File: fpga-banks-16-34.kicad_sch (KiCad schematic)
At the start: 45 parts, among them U1 ASFLMB-100.000MHZ-XY-T, U15 XC7K160T-FFG676, U8 PCA9517ADMR2G

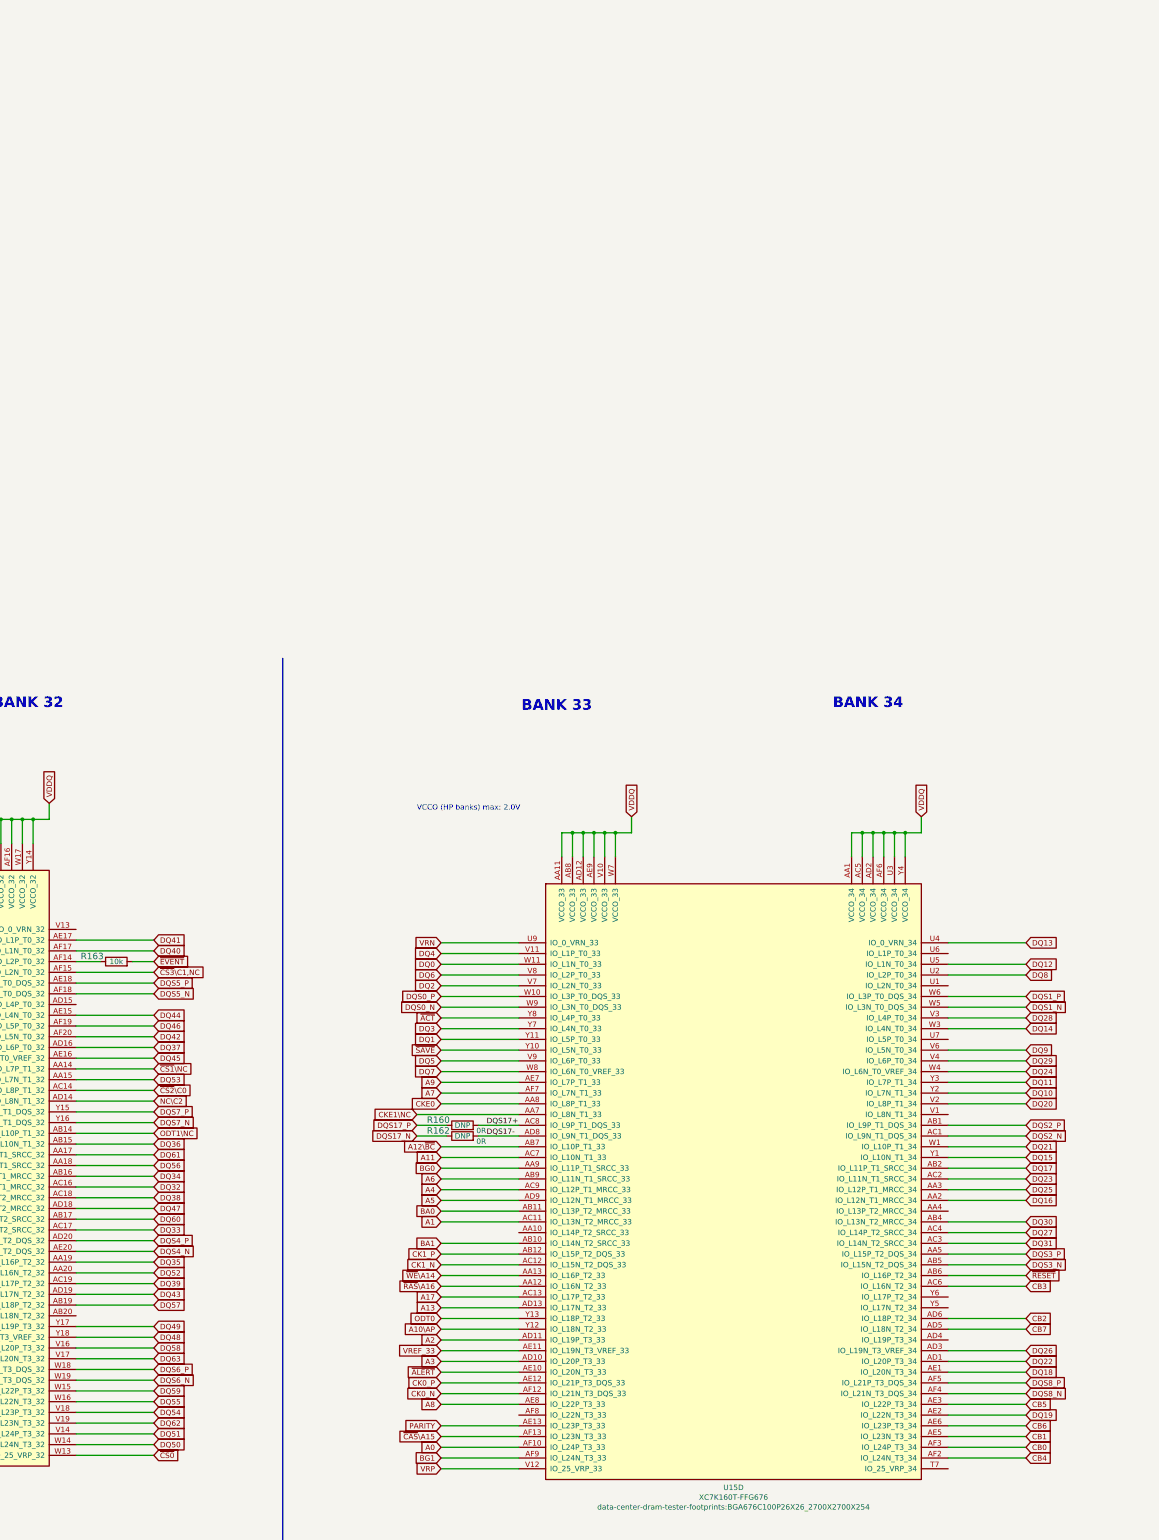
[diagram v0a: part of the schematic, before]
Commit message: Propose optimized DDR4 pinout for die[6..9], initial BGA fanout for bank 32
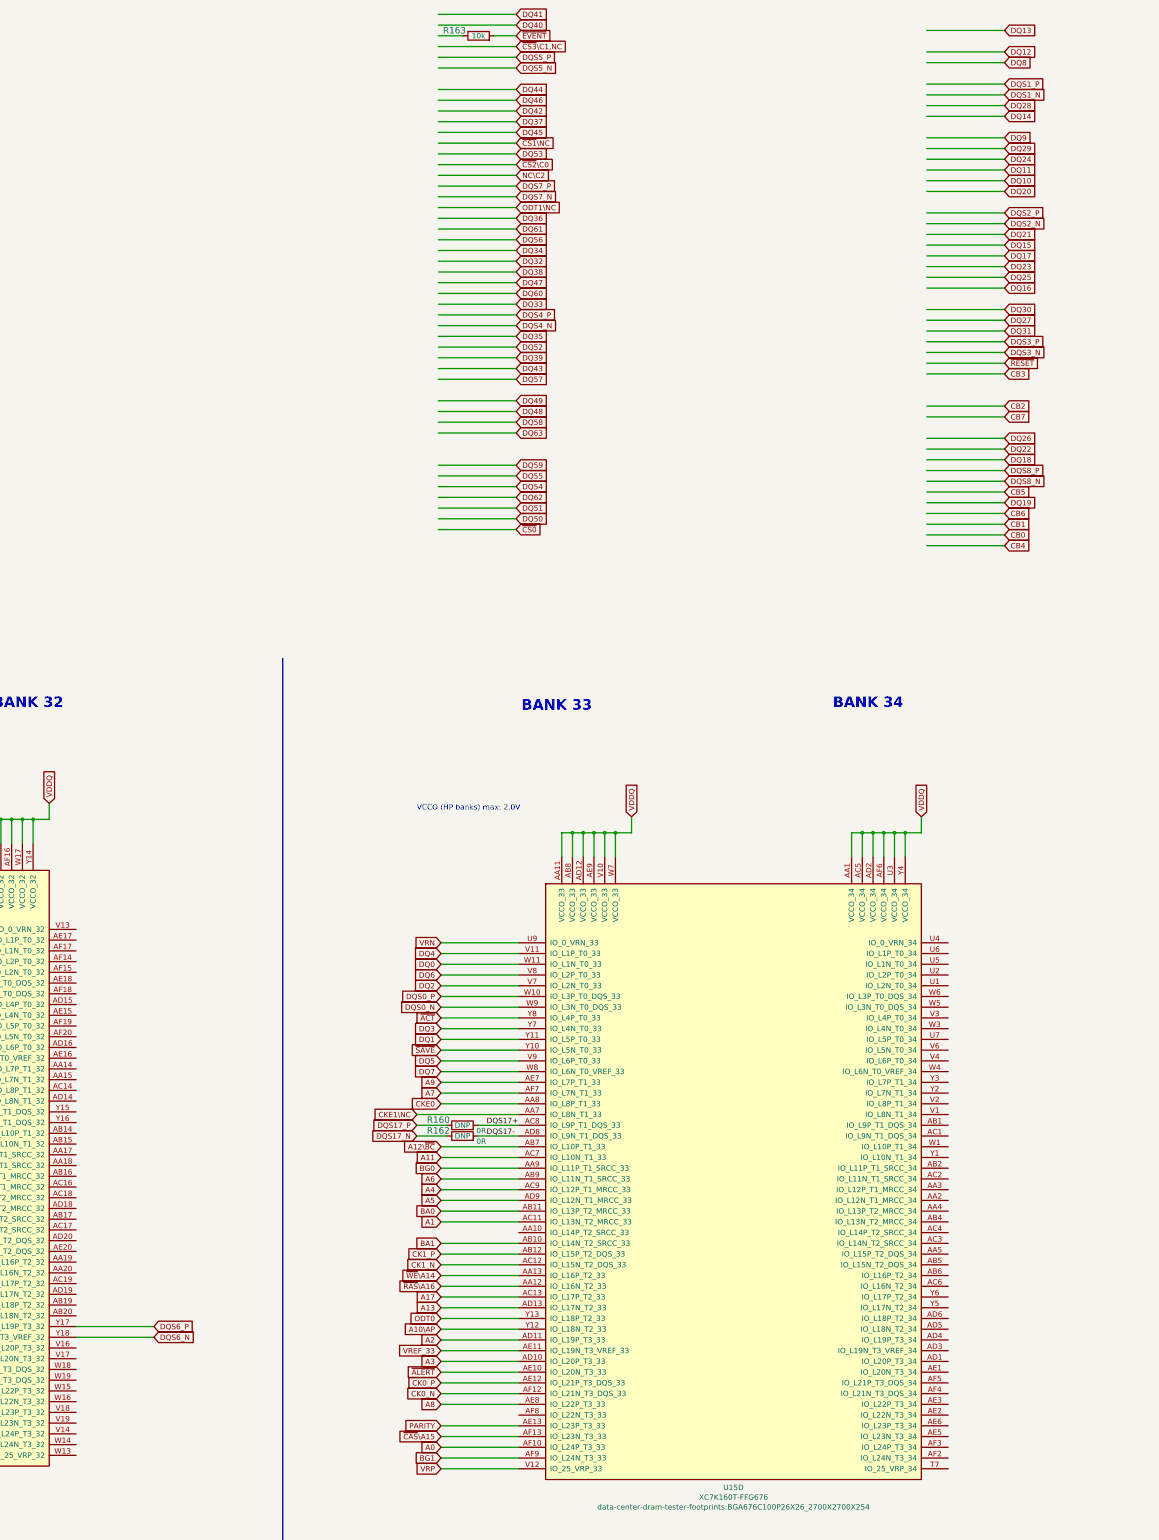
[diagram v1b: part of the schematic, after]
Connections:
- net CB0: no longer U15.AF3 (IO_L24P_T3_34)
- net CB1: no longer U15.AE5 (IO_L23N_T3_34)
- net CB2: no longer U15.AD6 (IO_L18P_T2_34)
- net CB3: no longer U15.AC6 (IO_L16N_T2_34)
- net CB4: no longer U15.AF2 (IO_L24N_T3_34)
- net CB5: no longer U15.AE3 (IO_L22P_T3_34)
- net CB6: no longer U15.AE6 (IO_L23P_T3_34)
- net CB7: no longer U15.AD5 (IO_L18N_T2_34)
- net DQ10: no longer U15.Y2 (IO_L7N_T1_34)
- net DQ11: no longer U15.Y3 (IO_L7P_T1_34)
- net DQ12: no longer U15.U5 (IO_L1N_T0_34)
- net DQ13: no longer U15.U4 (IO_0_VRN_34)
- net DQ14: no longer U15.W3 (IO_L4N_T0_34)
- net DQ15: no longer U15.Y1 (IO_L10N_T1_34)
- net DQ16: no longer U15.AA2 (IO_L12N_T1_MRCC_34)
- net DQ17: no longer U15.AB2 (IO_L11P_T1_SRCC_34)
- net DQ18: no longer U15.AE1 (IO_L20N_T3_34)
- net DQ19: no longer U15.AE2 (IO_L22N_T3_34)
- net DQ20: no longer U15.V2 (IO_L8P_T1_34)
- net DQ21: no longer U15.W1 (IO_L10P_T1_34)
- net DQ22: no longer U15.AD1 (IO_L20P_T3_34)
- net DQ23: no longer U15.AC2 (IO_L11N_T1_SRCC_34)
- net DQ24: no longer U15.W4 (IO_L6N_T0_VREF_34)
- net DQ25: no longer U15.AA3 (IO_L12P_T1_MRCC_34)
- net DQ26: no longer U15.AD3 (IO_L19N_T3_VREF_34)
- net DQ27: no longer U15.AC4 (IO_L14P_T2_SRCC_34)
- net DQ28: no longer U15.V3 (IO_L4P_T0_34)
- net DQ29: no longer U15.V4 (IO_L6P_T0_34)
- net DQ30: no longer U15.AB4 (IO_L13N_T2_MRCC_34)
- net DQ31: no longer U15.AC3 (IO_L14N_T2_SRCC_34)
- net DQ32: no longer U15.AC16 (IO_L12N_T1_MRCC_32)
- net DQ33: no longer U15.AC17 (IO_L14N_T2_SRCC_32)
- net DQ34: no longer U15.AB16 (IO_L12P_T1_MRCC_32)
- net DQ35: no longer U15.AA19 (IO_L16P_T2_32)
- net DQ36: no longer U15.AB15 (IO_L10N_T1_32)
- net DQ37: no longer U15.AD16 (IO_L6P_T0_32)
- net DQ38: no longer U15.AC18 (IO_L13P_T2_MRCC_32)
- net DQ39: no longer U15.AC19 (IO_L17P_T2_32)
- net DQ40: no longer U15.AF17 (IO_L1N_T0_32)
- net DQ41: no longer U15.AE17 (IO_L1P_T0_32)
- net DQ42: no longer U15.AF20 (IO_L5N_T0_32)
- net DQ43: no longer U15.AD19 (IO_L17N_T2_32)
- net DQ44: no longer U15.AE15 (IO_L4N_T0_32)
- net DQ45: no longer U15.AE16 (IO_L6N_T0_VREF_32)
- net DQ46: no longer U15.AF19 (IO_L5P_T0_32)
- net DQ47: no longer U15.AD18 (IO_L13N_T2_MRCC_32)
- net DQ48: no longer U15.Y18 (IO_L19N_T3_VREF_32)
- net DQ49: no longer U15.Y17 (IO_L19P_T3_32)
- net DQ50: no longer U15.W14 (IO_L24N_T3_32)
- net DQ51: no longer U15.V14 (IO_L24P_T3_32)
- net DQ52: no longer U15.AA20 (IO_L16N_T2_32)
- net DQ53: no longer U15.AA15 (IO_L7N_T1_32)
- net DQ54: no longer U15.V18 (IO_L23P_T3_32)
- net DQ55: no longer U15.W16 (IO_L22N_T3_32)
- net DQ56: no longer U15.AA18 (IO_L11N_T1_SRCC_32)
- net DQ57: no longer U15.AB19 (IO_L18P_T2_32)
- net DQ58: no longer U15.V16 (IO_L20P_T3_32)
- net DQ59: no longer U15.W15 (IO_L22P_T3_32)
- net DQ60: no longer U15.AB17 (IO_L14P_T2_SRCC_32)
- net DQ61: no longer U15.AA17 (IO_L11P_T1_SRCC_32)
- net DQ62: no longer U15.V19 (IO_L23N_T3_32)
- net DQ63: no longer U15.V17 (IO_L20N_T3_32)
- net DQ8: no longer U15.U2 (IO_L2P_T0_34)
- net DQ9: no longer U15.V6 (IO_L5N_T0_34)
- net DQS1_N: no longer U15.W5 (IO_L3N_T0_DQS_34)
- net DQS1_P: no longer U15.W6 (IO_L3P_T0_DQS_34)
- net DQS2_N: no longer U15.AC1 (IO_L9N_T1_DQS_34)
- net DQS2_P: no longer U15.AB1 (IO_L9P_T1_DQS_34)
- net DQS3_N: no longer U15.AB5 (IO_L15N_T2_DQS_34)
- net DQS3_P: no longer U15.AA5 (IO_L15P_T2_DQS_34)
- net DQS4_N: no longer U15.AE20 (IO_L15N_T2_DQS_32)
- net DQS4_P: no longer U15.AD20 (IO_L15P_T2_DQS_32)
- net DQS5_N: no longer U15.AF18 (IO_L3N_T0_DQS_32)
- net DQS5_P: no longer U15.AE18 (IO_L3P_T0_DQS_32)
- net DQS6_N: now also U15.Y18 (IO_L19N_T3_VREF_32); no longer U15.W19 (IO_L21N_T3_DQS_32)
- net DQS6_P: now also U15.Y17 (IO_L19P_T3_32); no longer U15.W18 (IO_L21P_T3_DQS_32)
- net DQS7_N: no longer U15.Y16 (IO_L9N_T1_DQS_32)
- net DQS7_P: no longer U15.Y15 (IO_L9P_T1_DQS_32)
- net DQS8_N: no longer U15.AF4 (IO_L21N_T3_DQS_34)
- net DQS8_P: no longer U15.AF5 (IO_L21P_T3_DQS_34)
- net NC\C2: no longer U15.AD14 (IO_L8N_T1_32)
- net ODT1\NC: no longer U15.AB14 (IO_L10P_T1_32)
- net ~{CS0}: no longer U15.W13 (IO_25_VRP_32)
- net ~{CS1}\NC: no longer U15.AA14 (IO_L7P_T1_32)
- net ~{CS2}\C0: no longer U15.AC14 (IO_L8P_T1_32)
- net ~{CS3}\C1,NC: no longer U15.AF15 (IO_L2N_T0_32)
- net ~{RESET}: no longer U15.AB6 (IO_L16P_T2_34)
- net at R163.1: no longer U15.AF14 (IO_L2P_T0_32)
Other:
- moved on the sheet: R163

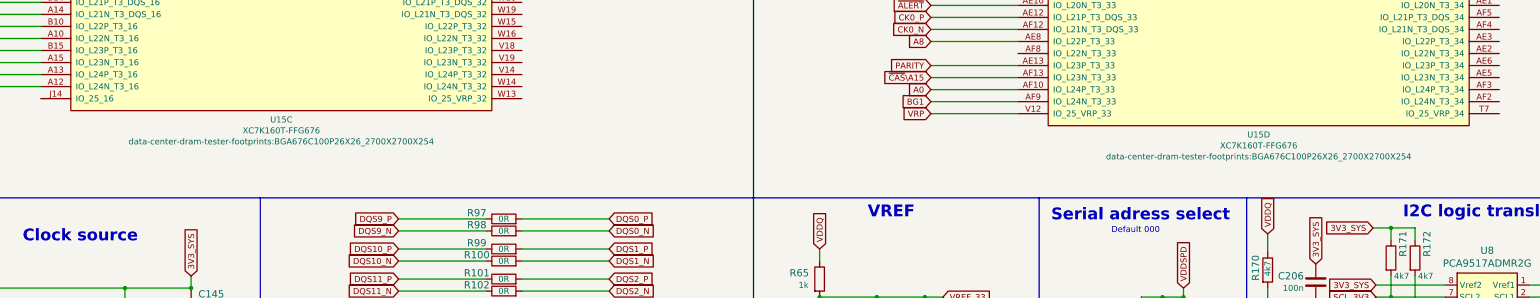
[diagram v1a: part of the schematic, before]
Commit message: Update FPGA symbol (die to pad length), initial fanout for die [1..4]
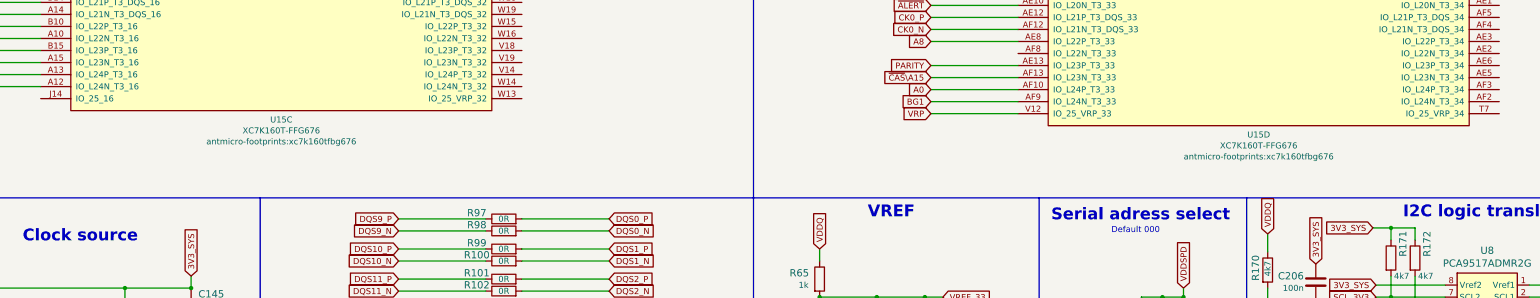
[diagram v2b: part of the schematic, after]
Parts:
- U15: footprint data-center-dram-tester-footprints:BGA676C100P26X26_2700X2700X254 -> antmicro-footprints:xc7k160tfbg676
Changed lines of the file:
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@@
     (property "Reference" "U15" (id 0) (at 96.52 205.105 0))
     (property "Value" "XC7K160T-FFG676" (id 1) (at 96.52 207.4164 0))
-    (property "Footprint" "data-center-dram-tester-footprints:BGA676C100P26X26_2700X2700X254" (id 2) (at 96.52 209.7278 0))
+    (property "Footprint" "antmicro-footprints:xc7k160tfbg676" (id 2) (at 96.52 209.7278 0))
     (property "Datasheet" "" (id 3) (at 96.52 129.54 0))
     (pin "AA21")
@@
     (property "Reference" "U15" (id 0) (at 302.895 208.28 0))
     (property "Value" "XC7K160T-FFG676" (id 1) (at 302.895 210.5914 0))
-    (property "Footprint" "data-center-dram-tester-footprints:BGA676C100P26X26_2700X2700X254" (id 2) (at 302.895 212.9028 0))
+    (property "Footprint" "antmicro-footprints:xc7k160tfbg676" (id 2) (at 302.895 212.9028 0))
     (property "Datasheet" "" (id 3) (at 302.895 132.715 0))
     (pin "AA21")

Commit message: Add new pinout for bank 32 and 34, create custom DRC rules for DDR, initial routing for die 6,7,9
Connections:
- net DQ0: now also U15.U6 (IO_L1P_T0_34); no longer U15.W11 (IO_L1N_T0_33)
- net DQ1: now also U15.V6 (IO_L5N_T0_34); no longer U15.Y11 (IO_L5P_T0_33)
- net DQ10: now also U15.AC3 (IO_L14N_T2_SRCC_34)
- net DQ11: now also U15.AC4 (IO_L14P_T2_SRCC_34)
- net DQ12: now also U15.W4 (IO_L6N_T0_VREF_34)
- net DQ13: now also U15.V4 (IO_L6P_T0_34)
- net DQ14: now also U15.AA4 (IO_L13P_T2_MRCC_34)
- net DQ15: now also U15.AB4 (IO_L13N_T2_MRCC_34)
- net DQ16: now also U15.V1 (IO_L8N_T1_34)
- net DQ17: now also U15.Y2 (IO_L7N_T1_34)
- net DQ18: now also U15.AC2 (IO_L11N_T1_SRCC_34)
- net DQ19: now also U15.AE1 (IO_L20N_T3_34)
- net DQ2: now also U15.AB6 (IO_L16P_T2_34); no longer U15.V7 (IO_L2N_T0_33)
- net DQ20: now also U15.U1 (IO_L2N_T0_34)
- net DQ21: now also U15.V2 (IO_L8P_T1_34)
- net DQ22: now also U15.AB2 (IO_L11P_T1_SRCC_34)
- net DQ23: now also U15.AD1 (IO_L20P_T3_34)
- net DQ24: now also U15.AE3 (IO_L22P_T3_34)
- net DQ25: now also U15.AF3 (IO_L24P_T3_34)
- net DQ26: now also U15.AD5 (IO_L18N_T2_34)
- net DQ27: now also U15.AD6 (IO_L18P_T2_34)
- net DQ28: now also U15.AE2 (IO_L22N_T3_34)
- net DQ29: now also U15.AF2 (IO_L24N_T3_34)
- net DQ3: now also U15.AC6 (IO_L16N_T2_34); no longer U15.Y7 (IO_L4N_T0_33)
- net DQ30: now also U15.AE5 (IO_L23N_T3_34)
- net DQ31: now also U15.AE6 (IO_L23P_T3_34)
- net DQ32: now also U15.AF15 (IO_L2N_T0_32)
- net DQ33: now also U15.AE16 (IO_L6N_T0_VREF_32)
- net DQ34: now also U15.AF19 (IO_L5P_T0_32)
- net DQ35: now also U15.AF20 (IO_L5N_T0_32)
- net DQ36: now also U15.AF14 (IO_L2P_T0_32)
- net DQ37: now also U15.AD14 (IO_L8N_T1_32)
- net DQ38: now also U15.AF18 (IO_L3N_T0_DQS_32)
- net DQ39: now also U15.AE18 (IO_L3P_T0_DQS_32)
- net DQ4: now also U15.U7 (IO_L5P_T0_34); no longer U15.V11 (IO_L1P_T0_33)
- net DQ40: now also U15.AB14 (IO_L10P_T1_32)
- net DQ41: now also U15.AD19 (IO_L17N_T2_32)
- net DQ42: now also U15.AC16 (IO_L12N_T1_MRCC_32)
- net DQ43: now also U15.AB15 (IO_L10N_T1_32)
- net DQ44: now also U15.AC14 (IO_L8P_T1_32)
- net DQ45: now also U15.AD16 (IO_L6P_T0_32)
- net DQ46: now also U15.AC19 (IO_L17P_T2_32)
- net DQ47: now also U15.AC17 (IO_L14N_T2_SRCC_32)
- net DQ48: now also U15.AA15 (IO_L7N_T1_32)
- net DQ49: now also U15.AB17 (IO_L14P_T2_SRCC_32)
- net DQ5: now also U15.U5 (IO_L1N_T0_34); no longer U15.V9 (IO_L6P_T0_33)
- net DQ50: now also U15.AA19 (IO_L16P_T2_32)
- net DQ51: now also U15.AA20 (IO_L16N_T2_32)
- net DQ52: now also U15.AA14 (IO_L7P_T1_32)
- net DQ53: now also U15.AB16 (IO_L12P_T1_MRCC_32)
- net DQ54: now also U15.AB19 (IO_L18P_T2_32)
- net DQ55: now also U15.AB20 (IO_L18N_T2_32)
- net DQ56: now also U15.Y15 (IO_L9P_T1_DQS_32)
- net DQ57: now also U15.Y16 (IO_L9N_T1_DQS_32)
- net DQ58: now also U15.W19 (IO_L21N_T3_DQS_32)
- net DQ59: now also U15.V19 (IO_L23N_T3_32)
- net DQ6: now also U15.AA5 (IO_L15P_T2_DQS_34); no longer U15.V8 (IO_L2P_T0_33)
- net DQ60: now also U15.W14 (IO_L24N_T3_32)
- net DQ61: now also U15.V14 (IO_L24P_T3_32)
- net DQ62: now also U15.W18 (IO_L21P_T3_DQS_32)
- net DQ63: now also U15.V18 (IO_L23P_T3_32)
- net DQ7: now also U15.AB5 (IO_L15N_T2_DQS_34); no longer U15.W8 (IO_L6N_T0_VREF_33)
- net DQ8: now also U15.U2 (IO_L2P_T0_34)
- net DQ9: now also U15.Y3 (IO_L7P_T1_34)
- net DQS0_N: now also U15.Y5 (IO_L17N_T2_34); no longer U15.W9 (IO_L3N_T0_DQS_33)
- net DQS0_P: now also U15.Y6 (IO_L17P_T2_34); no longer U15.W10 (IO_L3P_T0_DQS_33)
- net DQS10_N: now also U15.W3 (IO_L4N_T0_34)
- net DQS10_P: now also U15.V3 (IO_L4P_T0_34)
- net DQS11_N: now also U15.Y1 (IO_L10N_T1_34)
- net DQS11_P: now also U15.W1 (IO_L10P_T1_34)
- net DQS12_N: now also U15.AD3 (IO_L19N_T3_VREF_34)
- net DQS12_P: now also U15.AD4 (IO_L19P_T3_34)
- net DQS13_N: now also U15.AE15 (IO_L4N_T0_32)
- net DQS13_P: now also U15.AD15 (IO_L4P_T0_32)
- net DQS14_N: now also U15.AE20 (IO_L15N_T2_DQS_32)
- net DQS14_P: now also U15.AD20 (IO_L15P_T2_DQS_32)
- net DQS15_N: now also U15.AA18 (IO_L11N_T1_SRCC_32)
- net DQS15_P: now also U15.AA17 (IO_L11P_T1_SRCC_32)
- net DQS16_N: now also U15.W16 (IO_L22N_T3_32)
- net DQS16_P: now also U15.W15 (IO_L22P_T3_32)
- net DQS17+: no longer U15.AC8 (IO_L9P_T1_DQS_33)
- net DQS17-: no longer U15.AD8 (IO_L9N_T1_DQS_33)
- net DQS1_N: now also U15.AA2 (IO_L12N_T1_MRCC_34)
- net DQS1_P: now also U15.AA3 (IO_L12P_T1_MRCC_34)
- net DQS2_N: now also U15.AC1 (IO_L9N_T1_DQS_34)
- net DQS2_P: now also U15.AB1 (IO_L9P_T1_DQS_34)
- net DQS3_N: now also U15.AF4 (IO_L21N_T3_DQS_34)
- net DQS3_P: now also U15.AF5 (IO_L21P_T3_DQS_34)
- net DQS4_N: now also U15.AF17 (IO_L1N_T0_32)
- net DQS4_P: now also U15.AE17 (IO_L1P_T0_32)
- net DQS5_N: now also U15.AD18 (IO_L13N_T2_MRCC_32)
- net DQS5_P: now also U15.AC18 (IO_L13P_T2_MRCC_32)
- net DQS7_N: now also U15.V17 (IO_L20N_T3_32)
- net DQS7_P: now also U15.V16 (IO_L20P_T3_32)
- net DQS9_N: now also U15.W5 (IO_L3N_T0_DQS_34)
- net DQS9_P: now also U15.W6 (IO_L3P_T0_DQS_34)
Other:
- moved on the sheet: R160, R162, R163

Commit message: Progress in DDR routing
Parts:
- removed R100, R101, R102, R103, R104, R105, R106, R107, R108, R109, R110, R111, R112, R113, R114, R160, R162, R97, R98, R99: R_0R_0201, data-center-dram-tester-footprints:0201-res, symbol data-center-dram-tester:R_0R_0201
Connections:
- net DQ56 is gone; now on net DQ61: U15.Y15 (IO_L9P_T1_DQS_32)
- net DQ61: no longer U15.V14 (IO_L24P_T3_32)
- net ~{RESET}: now also U15.AF8 (IO_L22N_T3_33)
